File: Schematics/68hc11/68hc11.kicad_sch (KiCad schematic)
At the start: 50 parts, among them J1 DC 5 Volts, J2 DB9_Female, J3 Conn_01x10_Male, J4 Conn_01x10_Male, J5 Conn_01x10_Male, J6 Conn_01x10_Male, J7 Conn_01x10_Male, SW1 Reset, U1 MC68HC11A1CC-PLLC, U10 MCP100-270D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

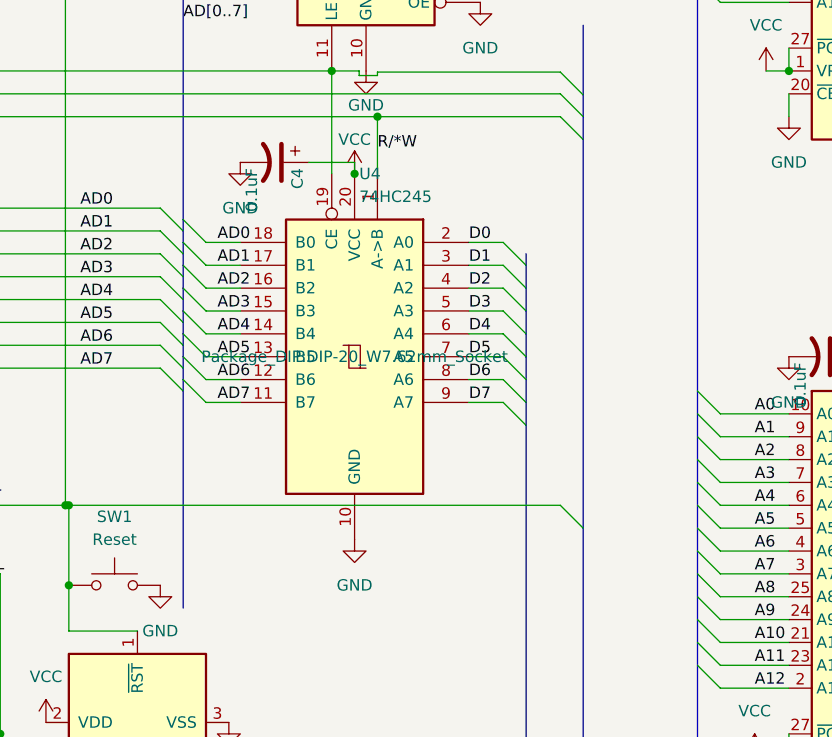
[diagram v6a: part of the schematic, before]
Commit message: Updated chip footprints and generated new vBOM
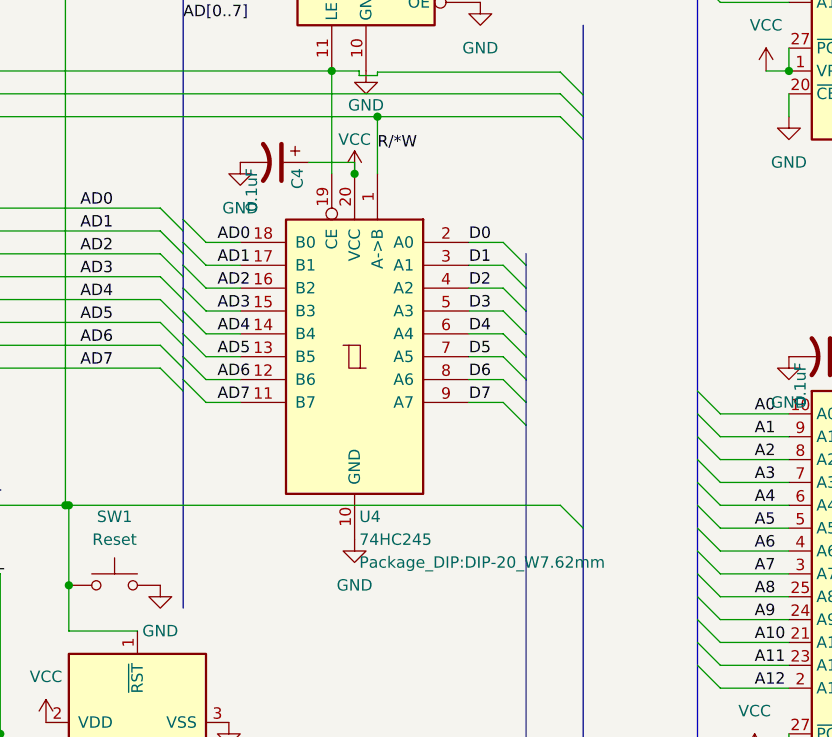
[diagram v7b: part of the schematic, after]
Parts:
- U11, U5, U9: footprint Package_DIP:DIP-16_W7.62mm_Socket -> Package_DIP:DIP-16_W7.62mm
- U12, U13, U14, U15: footprint Package_DIP:DIP-14_W7.62mm_Socket -> Package_DIP:DIP-14_W7.62mm
- U13: footprint (none) -> Package_DIP:DIP-14_W7.62mm
- U2: footprint Package_DIP:DIP-40_W15.24mm_Socket -> Package_DIP:DIP-40_W15.24mm
- U3, U4: footprint Package_DIP:DIP-20_W7.62mm_Socket -> Package_DIP:DIP-20_W7.62mm
- U6, U7, U8: footprint Package_DIP:DIP-28_W15.24mm_Socket -> Package_DIP:DIP-28_W15.24mm

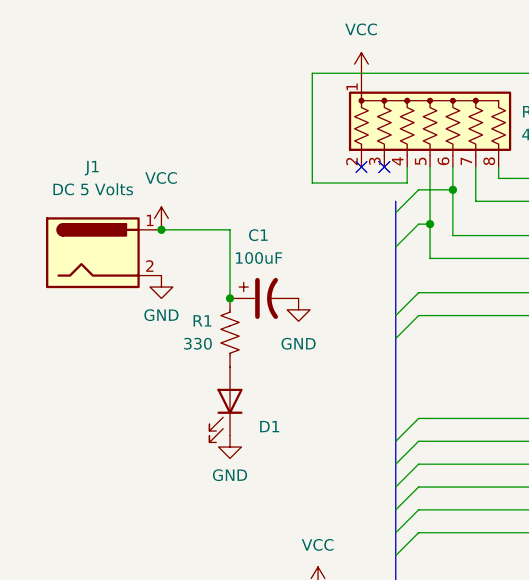
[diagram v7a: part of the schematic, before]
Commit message: Updated power to micro usb b receptical
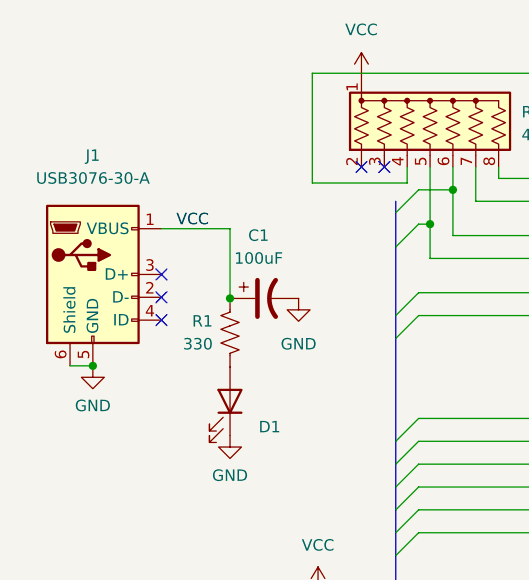
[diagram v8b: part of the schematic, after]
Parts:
- J1: value DC 5 Volts -> USB3076-30-A; footprint digikey-footprints:Barrel_Jack_5.5mmODx2.1mmID_PJ-102A -> digikey-footprints:USB_Micro_B_Female_10118193-0001LF; symbol Connector:Jack-DC -> Connector:USB_B_Micro
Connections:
- net GND: now also J1.5 (GND), J1.6 (Shield); no longer J1.2
- no-connect marks 14 -> 17
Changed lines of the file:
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@@
   (junction (at 287.02 60.96) (diameter 0) (color 0 0 0 0)
   )
-  (junction (at 127 144.78) (diameter 0) (color 0 0 0 0)
+  (junction (at 23.495 47.498) (diameter 0) (color 0 0 0 0)
   )
-  (junction (at 31.115 32.385) (diameter 0) (color 0 0 0 0)
+  (junction (at 127 144.78) (diameter 0) (color 0 0 0 0)
   )
   (junction (at 139.7 205.74) (diameter 0) (color 0 0 0 0)
@@
   (no_connect (at 149.86 212.09))
   (no_connect (at 149.86 222.25))
+  (no_connect (at 31.115 39.878))
+  (no_connect (at 31.115 37.338))
+  (no_connect (at 31.115 42.418))
   (no_connect (at 55.88 25.4))
   (no_connect (at 53.34 25.4))
@@
     (stroke (width 0) (type default) (color 0 0 0 0))
   )
+  (wire (pts (xy 20.955 47.498) (xy 23.495 47.498))
+    (stroke (width 0) (type default) (color 0 0 0 0))
+  )
   (wire (pts (xy 59.69 27.94) (xy 63.5 27.94))
     (stroke (width 0) (type default) (color 0 0 0 0))
@@
     (stroke (width 0) (type default) (color 0 0 0 0))
   )
-  (wire (pts (xy 38.735 32.385) (xy 38.735 40.005))
-    (stroke (width 0) (type default) (color 0 0 0 0))
-  )
   (wire (pts (xy 233.68 276.86) (xy 236.22 276.86))
     (stroke (width 0) (type default) (color 0 0 0 0))
@@
     (stroke (width 0) (type default) (color 0 0 0 0))
   )
-  (wire (pts (xy 31.115 32.385) (xy 38.735 32.385))
-    (stroke (width 0) (type default) (color 0 0 0 0))
-  )
   (bus (pts (xy 242.57 181.61) (xy 242.57 184.15))
     (stroke (width 0) (type default) (color 0 0 0 0))
@@
     (stroke (width 0) (type default) (color 0 0 0 0))
   )
+  (wire (pts (xy 38.735 32.258) (xy 38.735 40.005))
+    (stroke (width 0) (type default) (color 0 0 0 0))
+  )
   (wire (pts (xy 63.5 25.4) (xy 63.5 27.94))
     (stroke (width 0) (type default) (color 0 0 0 0))
@@
     (stroke (width 0) (type default) (color 0 0 0 0))
   )
+  (wire (pts (xy 31.115 32.258) (xy 38.735 32.258))
+    (stroke (width 0) (type default) (color 0 0 0 0))
+  )
   (bus (pts (xy 242.57 179.07) (xy 242.57 181.61))
     (stroke (width 0) (type default) (color 0 0 0 0))
@@
     (stroke (width 0) (type default) (color 0 0 0 0))
   )
-  (wire (pts (xy 30.988 32.385) (xy 31.115 32.385))
-    (stroke (width 0) (type default) (color 0 0 0 0))
-  )
   (wire (pts (xy 179.07 96.52) (xy 182.88 96.52))
     (stroke (width 0) (type default) (color 0 0 0 0))
@@
     (effects (font (size 1.27 1.27)) (justify left bottom))
   )
+  (label "VCC" (at 32.766 32.258 0)
+    (effects (font (size 1.27 1.27)) (justify left bottom))
+  )
   (label "PPB0" (at 314.96 220.98 0)
     (effects (font (size 1.27 1.27)) (justify left bottom))
@@
     (pin "1")
   )
-  (symbol (lib_id "power:GND") (at 31.115 37.465 0) (unit 1)
+  (symbol (lib_id "power:GND") (at 23.495 47.498 0) (unit 1)
     (in_bom yes) (on_board yes) (fields_autoplaced)
-    (property "Reference" "#PWR01" (id 0) (at 31.115 43.815 0)
+    (property "Reference" "#PWR01" (id 0) (at 23.495 53.848 0)
       (effects (font (size 1.27 1.27)) hide)
     )
-    (property "Value" "GND" (id 1) (at 31.115 41.91 0))
-    (property "Footprint" "Connector_BarrelJack:BarrelJack_CUI_PJ-063AH_Horizontal_CircularHoles" (id 2) (at 31.115 37.465 0)
+    (property "Value" "GND" (id 1) (at 23.495 51.943 0))
+    (property "Footprint" "Connector_BarrelJack:BarrelJack_CUI_PJ-063AH_Horizontal_CircularHoles" (id 2) (at 23.495 47.498 0)
       (effects (font (size 1.27 1.27)) hide)
     )
-    (property "Datasheet" "" (id 3) (at 31.115 37.465 0)
+    (property "Datasheet" "" (id 3) (at 23.495 47.498 0)
       (effects (font (size 1.27 1.27)) hide)
     )
@@
     (pin "9")
   )
-  (symbol (lib_id "Connector:Jack-DC") (at 23.495 34.925 0) (unit 1)
+  (symbol (lib_id "Connector:USB_B_Micro") (at 23.495 37.338 0) (unit 1)
     (in_bom yes) (on_board yes) (fields_autoplaced)
-    (property "Reference" "J1" (id 0) (at 23.495 25.4 0))
-    (property "Value" "DC 5 Volts" (id 1) (at 23.495 27.94 0))
-    (property "Footprint" "digikey-footprints:Barrel_Jack_5.5mmODx2.1mmID_PJ-102A" (id 2) (at 24.765 35.941 0)
+    (property "Reference" "J1" (id 0) (at 23.495 24.13 0))
+    (property "Value" "USB3076-30-A" (id 1) (at 23.495 26.67 0))
+    (property "Footprint" "digikey-footprints:USB_Micro_B_Female_10118193-0001LF" (id 2) (at 27.305 38.608 0)
       (effects (font (size 1.27 1.27)) hide)
     )
-    (property "Datasheet" "~" (id 3) (at 24.765 35.941 0)
+    (property "Datasheet" "~" (id 3) (at 27.305 38.608 0)
       (effects (font (size 1.27 1.27)) hide)
     )
     (pin "1")
     (pin "2")
+    (pin "3")
+    (pin "4")
+    (pin "5")
+    (pin "6")
   )
   (symbol (lib_id "Device:C_Polarized_US") (at 384.81 127 270) (unit 1)
@@
     (pin "2")
   )
-  (symbol (lib_id "power:VCC") (at 31.115 32.385 0) (unit 1)
-    (in_bom yes) (on_board yes) (fields_autoplaced)
-    (property "Reference" "#PWR0135" (id 0) (at 31.115 36.195 0)
-      (effects (font (size 1.27 1.27)) hide)
-    )
-    (property "Value" "VCC" (id 1) (at 31.115 26.67 0))
-    (property "Footprint" "" (id 2) (at 31.115 32.385 0)
-      (effects (font (size 1.27 1.27)) hide)
-    )
-    (property "Datasheet" "" (id 3) (at 31.115 32.385 0)
-      (effects (font (size 1.27 1.27)) hide)
-    )
-    (pin "1")
-  )
   (symbol (lib_id "Device:C_Polarized_US") (at 158.75 15.24 270) (unit 1)
     (in_bom yes) (on_board yes)
@@
       (reference "#PWR0134") (unit 1) (value "GND") (footprint "")
     )
-    (path "/cff43ac9-e6e1-46ac-a513-7022be2adf5a"
-      (reference "#PWR0135") (unit 1) (value "VCC") (footprint "")
-    )
     (path "/a6e490e6-0f87-4d7d-bfe7-a16680c84571"
       (reference "#PWR0136") (unit 1) (value "GND") (footprint "")
@@
     )
     (path "/cd706897-8387-41f6-bf63-ac166aa97193"
-      (reference "J1") (unit 1) (value "DC 5 Volts") (footprint "digikey-footprints:Barrel_Jack_5.5mmODx2.1mmID_PJ-102A")
+      (reference "J1") (unit 1) (value "USB3076-30-A") (footprint "digikey-footprints:USB_Micro_B_Female_10118193-0001LF")
     )
     (path "/b08b0f27-3b77-4f78-b1af-b66a2e38028e"
